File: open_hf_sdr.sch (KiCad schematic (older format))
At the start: 0 parts

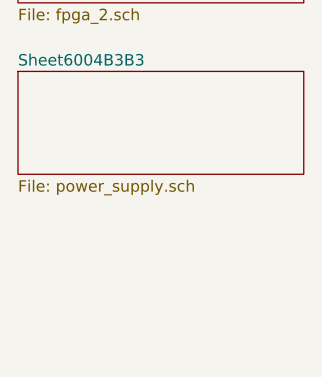
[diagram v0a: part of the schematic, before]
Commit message: FPGA supply notes
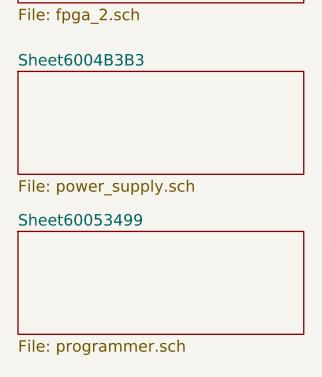
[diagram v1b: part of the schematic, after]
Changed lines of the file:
@@
 $Descr A4 11693 8268
 encoding utf-8
-Sheet 1 12
+Sheet 1 14
 Title "Open HF SDR FPGA Sheet"
 Date "2021-01-16"
@@
 F1 "power_supply.sch" 50
 $EndSheet
+$Sheet
+S 1150 3900 1250 450
+U 6005349A
+F0 "Sheet60053499" 50
+F1 "programmer.sch" 50
+$EndSheet
 $EndSCHEMATC

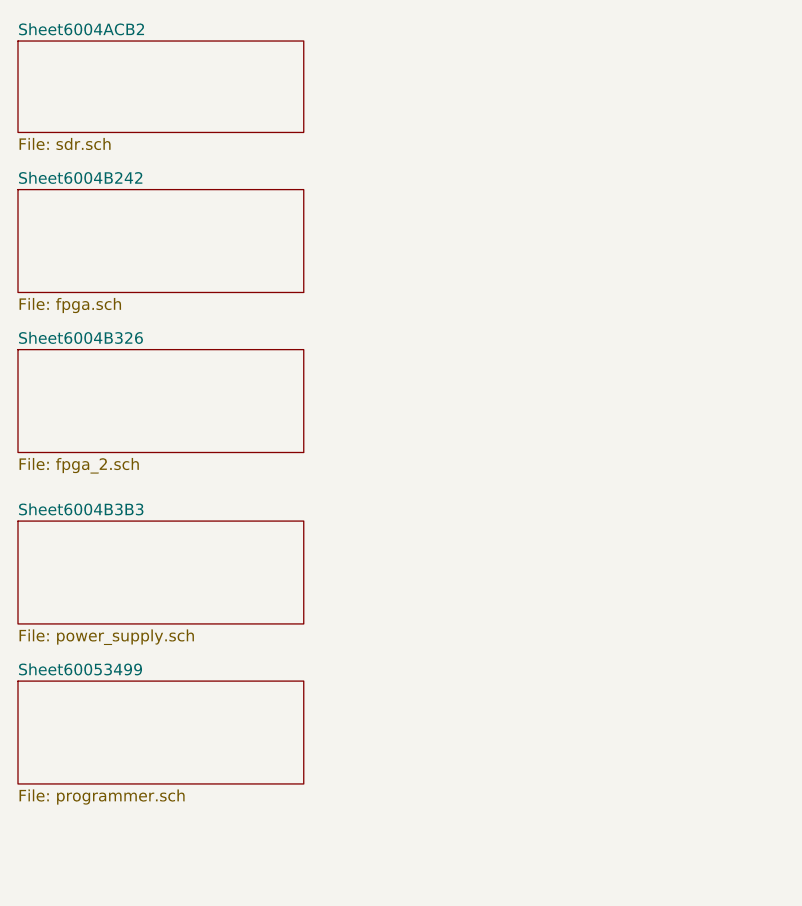
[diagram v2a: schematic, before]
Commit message: SDR-FPGA Interface v0
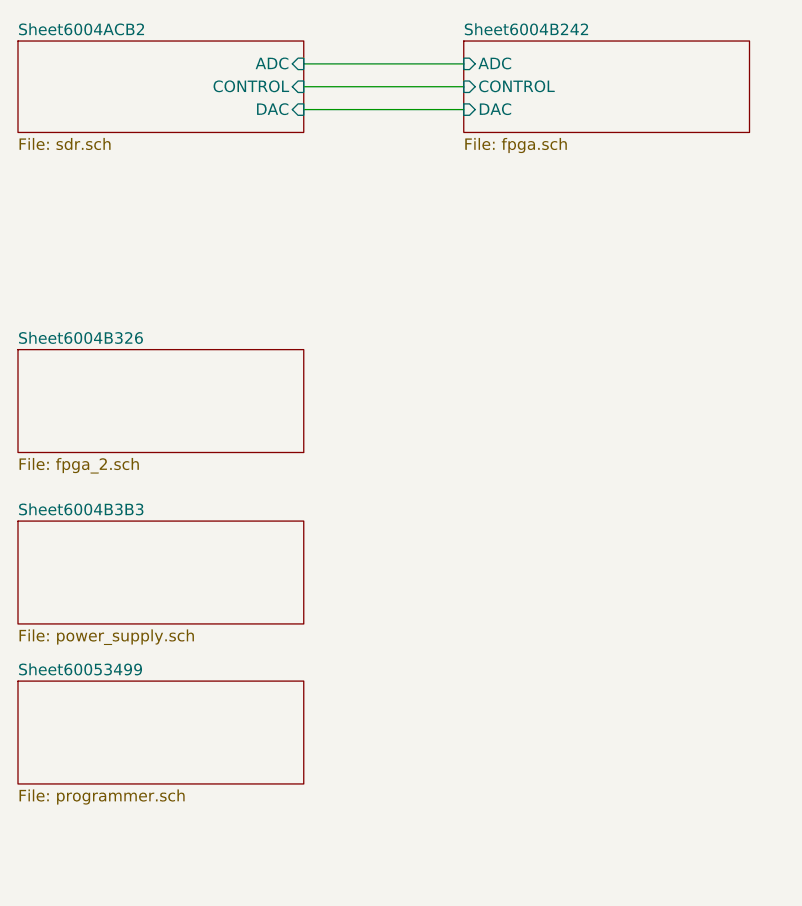
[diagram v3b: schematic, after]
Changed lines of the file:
@@
 F0 "Sheet6004ACB2" 50
 F1 "sdr.sch" 50
+F2 "ADC" I R 2400 1200 50
+F3 "DAC" I R 2400 1400 50
+F4 "CONTROL" I R 2400 1300 50
 $EndSheet
 $Sheet
-S 1150 1750 1250 450
+S 3100 1100 1250 400
 U 6004B243
 F0 "Sheet6004B242" 50
 F1 "fpga.sch" 50
+F2 "ADC" I L 3100 1200 50
+F3 "DAC" I L 3100 1400 50
+F4 "CONTROL" I L 3100 1300 50
 $EndSheet
 $Sheet
@@
 F1 "programmer.sch" 50
 $EndSheet
+Wire Wire Line
+	2400 1200 3100 1200
+Wire Wire Line
+	2400 1400 3100 1400
+Wire Wire Line
+	3100 1300 2400 1300
 $EndSCHEMATC

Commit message: Begin the implementation of Human in-out, a few small changes
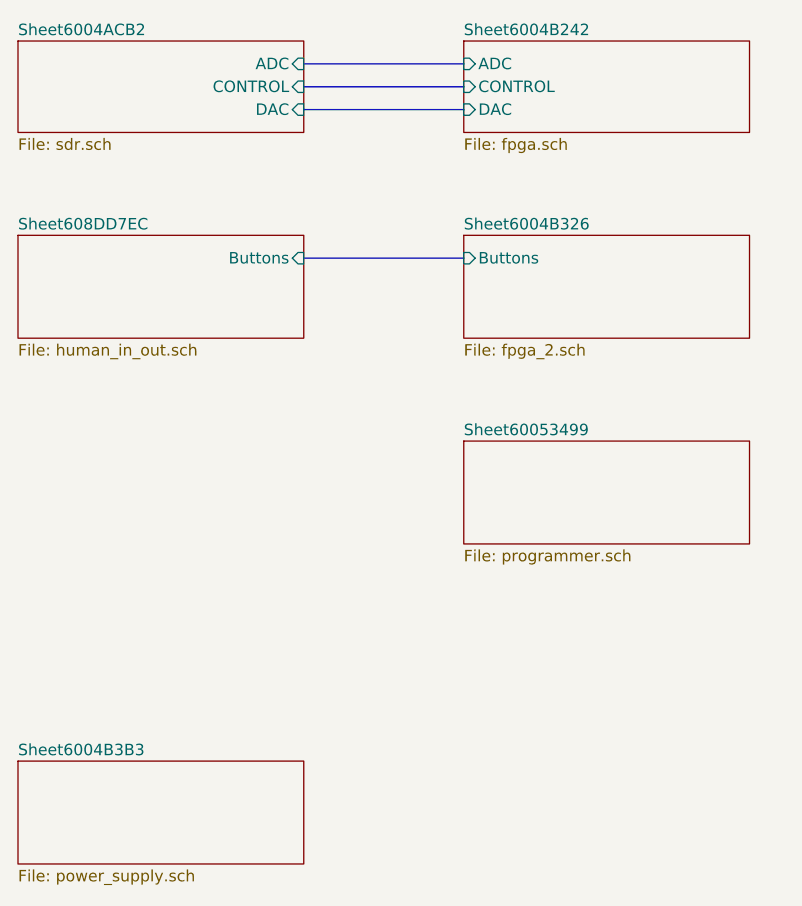
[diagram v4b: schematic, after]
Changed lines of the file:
@@
 $Descr A4 11693 8268
 encoding utf-8
-Sheet 1 16
+Sheet 1 17
 Title "Open HF SDR FPGA Sheet"
 Date "2021-01-16"
@@
 $EndSheet
 $Sheet
-S 1150 2450 1250 450
+S 3100 1950 1250 450
 U 6004B327
 F0 "Sheet6004B326" 50
 F1 "fpga_2.sch" 50
+F2 "Buttons" I L 3100 2050 50
 $EndSheet
 $Sheet
-S 1150 3200 1250 450
+S 1150 4250 1250 450
 U 6004B3B4
 F0 "Sheet6004B3B3" 50
@@
 $EndSheet
 $Sheet
-S 1150 3900 1250 450
+S 3100 2850 1250 450
 U 6005349A
 F0 "Sheet60053499" 50
 F1 "programmer.sch" 50
 $EndSheet
-Wire Wire Line
+$Sheet
+S 1150 1950 1250 450
+U 608DD7ED
+F0 "Sheet608DD7EC" 50
+F1 "human_in_out.sch" 50
+F2 "Buttons" I R 2400 2050 50
+$EndSheet
+Wire Bus Line
+	2400 2050 3100 2050
+Wire Bus Line
+	2400 1400 3100 1400
+Wire Bus Line
+	2400 1300 3100 1300
+Wire Bus Line
 	2400 1200 3100 1200
-Wire Wire Line
-	2400 1400 3100 1400
-Wire Wire Line
-	3100 1300 2400 1300
 $EndSCHEMATC

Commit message: Add USB-FPGA bus labels
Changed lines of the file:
@@
 F0 "Sheet60053499" 50
 F1 "programmer.sch" 50
+F2 "SDR_CONTROL" I L 3100 2950 50
+F3 "T_DATA" I L 3100 3050 50
+F4 "R_DATA" I L 3100 3150 50
 $EndSheet
 $Sheet

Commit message: connect leds to fpga
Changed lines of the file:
@@
 F1 "fpga_2.sch" 50
 F2 "Buttons" I L 3100 2050 50
+F3 "Leds" O L 3100 2150 50
 $EndSheet
 $Sheet
@@
 F0 "Sheet608DD7EC" 50
 F1 "human_in_out.sch" 50
-F2 "Buttons" I R 2400 2050 50
+F2 "Leds" I R 2400 2150 50
+F3 "Buttons" O R 2400 2050 50
 $EndSheet
 Wire Bus Line
@@
 Wire Bus Line
 	2400 1200 3100 1200
+Wire Bus Line
+	2400 2150 3100 2150
 $EndSCHEMATC

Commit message: Connect USB buses to the FPGA
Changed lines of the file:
@@
 F3 "DAC" I L 3100 1400 50
 F4 "CONTROL" I L 3100 1300 50
+F5 "SDR_CONTROL" I R 4350 1200 50
 $EndSheet
 $Sheet
@@
 F2 "Buttons" I L 3100 2050 50
 F3 "Leds" O L 3100 2150 50
+F4 "T_DATA" I R 4350 2050 50
+F5 "R_DATA" I R 4350 2150 50
 $EndSheet
 $Sheet
@@
 F0 "Sheet60053499" 50
 F1 "programmer.sch" 50
-F2 "SDR_CONTROL" I L 3100 2950 50
-F3 "T_DATA" I L 3100 3050 50
-F4 "R_DATA" I L 3100 3150 50
+F2 "SDR_CONTROL" I R 4350 3150 50
+F3 "T_DATA" I R 4350 3050 50
+F4 "R_DATA" I R 4350 2950 50
 $EndSheet
 $Sheet
@@
 Wire Bus Line
 	2400 2150 3100 2150
+Wire Bus Line
+	4350 2150 4400 2150
+Wire Bus Line
+	4400 2150 4400 2950
+Wire Bus Line
+	4400 2950 4350 2950
+Wire Bus Line
+	4350 2050 4450 2050
+Wire Bus Line
+	4450 2050 4450 3050
+Wire Bus Line
+	4450 3050 4350 3050
+Wire Bus Line
+	4350 3150 4500 3150
+Wire Bus Line
+	4500 3150 4500 1200
+Wire Bus Line
+	4500 1200 4350 1200
 $EndSCHEMATC
